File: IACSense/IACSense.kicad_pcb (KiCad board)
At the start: 2 copper layers, 56.6 x 87.4 mm, 75 parts, among them P1 IN, P2 OUT, P3 zcd, P4 event, P5 Prog, P7 I2C, U1 MCP39F521, U2 MCP970x, U3 MCP1754ST-3302E/CB, U4 PIC16F18323_QFN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

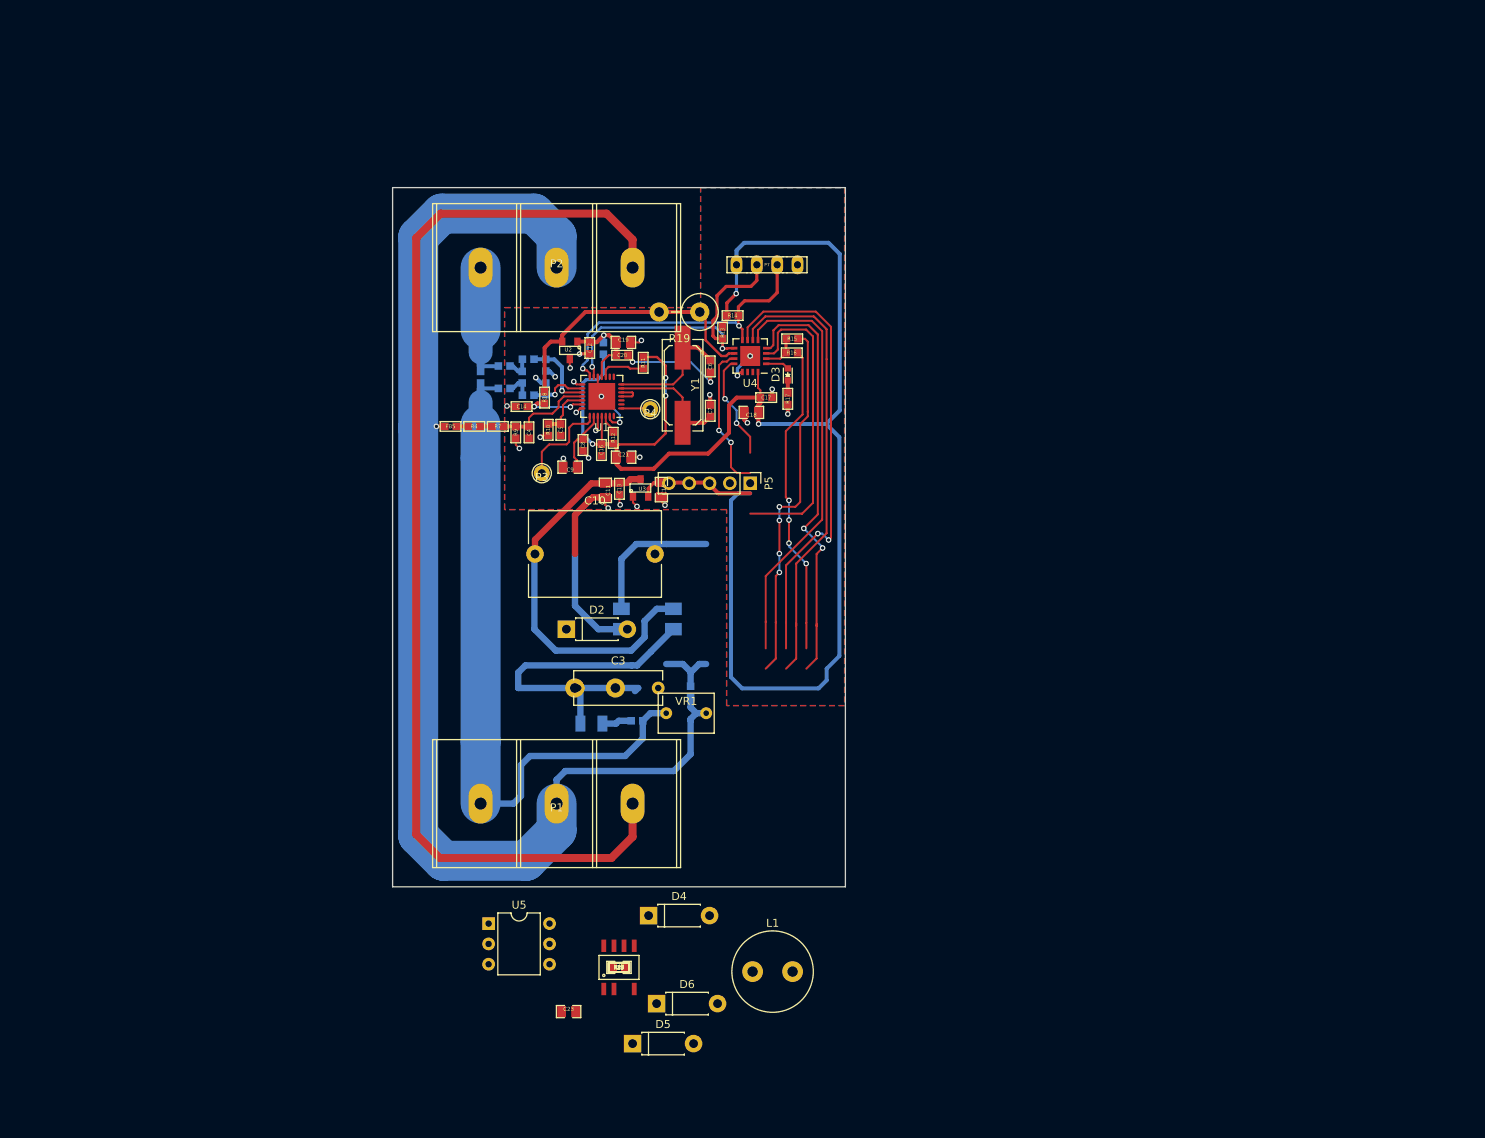
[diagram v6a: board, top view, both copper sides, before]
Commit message: Update IACSense layout
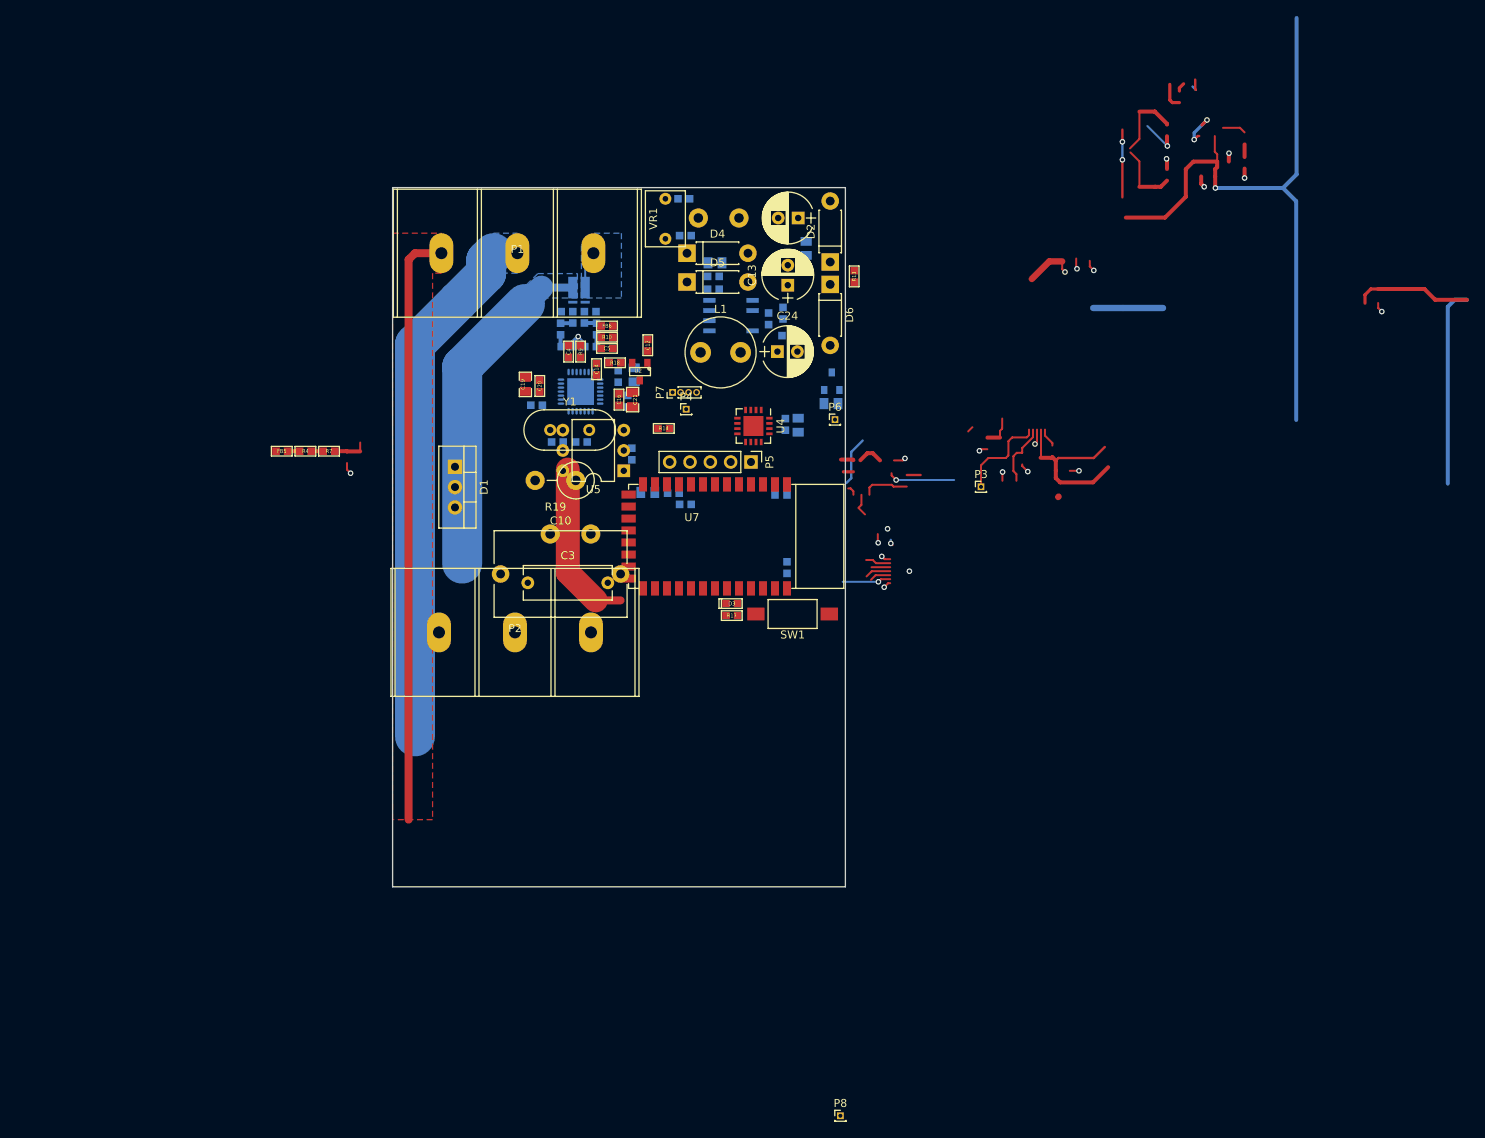
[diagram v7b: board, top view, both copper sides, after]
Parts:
- removed R15: nc, Yame_library:SM0603-MR
- removed R16: 0, Yame_library:SM0603-MR
- added C24: 100u_25V, Capacitors_THT:CP_Radial_D6.3mm_P2.50mm, F.Cu at (228.1, 72.5)
- added C25: C, Yame_library:SM0603-MR, B.Cu at (216.6, 91.6)
- added P6: +3.3v, Pin_Headers:Pin_Header_Straight_1x01_Pitch1.00mm, F.Cu at (235.3, 81.0)
- added P8: Test, Pin_Headers:Pin_Header_Straight_1x01_Pitch1.00mm, F.Cu at (236.0, 168.0)
- added R21: 100, Yame_library:SM0805-MR, B.Cu at (231.7, 59.6)
- added R26: R, Yame_library:SM0603-MR, B.Cu at (229.3, 89.7)
- added R27: R, Yame_library:SM0603-MR, B.Cu at (227.8, 89.7)
- added R28: R, Yame_library:SM0603-MR, B.Cu at (215.1, 90.2)
- added R29: R, Yame_library:SM0603-MR, B.Cu at (229.3, 99.5)
- added SW1: SW_Push, Buttons_Switches_SMD:SW_SPST_FSMSM, F.Cu at (230.0, 105.3)
- added U7: HC-05_Bluetooth_Module, Yame_library:HM-10_BLE, F.Cu at (211.3, 89.1)
- C11: value 1u_400V -> ECA-2GM010; footprint Yame_library:SM0805-MR -> Capacitors_THT:CP_Radial_D6.3mm_P2.50mm
- C13: value 1u_400V -> ECA-2GM010; footprint Yame_library:SM0603-MR -> Capacitors_THT:CP_Radial_D6.3mm_P2.50mm
- C15, C17, C18, C22, C23, C26, C6, C7, C8, C9, R22, R23, R24, R25, U1, U6: moved to B.Cu
- D1: value Q_TRIAC_AAG -> Q_TRIAC; footprint Yame_library:MBxS -> TO_SOT_Packages_THT:TO-220-3_Vertical; moved to F.Cu
- D3: footprint LEDs:LED_0603 -> Yame_library:SM0603-LED-MR
- L1: footprint Inductors_THT:L_Radial_D10.0mm_P5.00mm_Fastron_07M -> Inductors_THT:L_Radial_D8.7mm_P5.00mm_Fastron_07HCP
- P3, P4: footprint Yame_library:Test_Point_T_H -> Pin_Headers:Pin_Header_Straight_1x01_Pitch1.00mm
- P7: footprint Yame_library:HE10_14-4C-2.54-MR -> Pin_Headers:Pin_Header_Straight_1x04_Pitch1.00mm
- R11, R12: value 1k -> 4k7; moved to B.Cu
- R2: footprint Yame_library:SM1206-MR -> FC4L32
- R20: footprint Yame_library:SM0603-MR -> Resistors_THT:R_Axial_DIN0414_L11.9mm_D4.5mm_P5.08mm_Vertical
- U3: value MCP1754ST-3302E/CB -> AP2120N-3.3TRG1; moved to B.Cu
- Y1: footprint Crystals:Q_49U3HMS -> Crystals:Crystal_HC49-4H_Vertical
- moved D5 95.4 mm to (216.8, 63.8)
- moved C23 95.4 mm to (220.3, 61.4), turned to 180 degrees
- moved D6 92.5 mm to (234.7, 64.1), turned to 270 degrees
- moved R22 87.2 mm to (220.1, 63.1), turned to 180 degrees
- moved C22 85.6 mm to (220.1, 64.7), turned to 180 degrees
- moved R24 84.3 mm to (228.8, 67.7), turned to 270 degrees
- moved R23 83.2 mm to (227.0, 68.4), turned to 270 degrees
- moved D4 82.9 mm to (216.8, 60.2)
- moved U6 82.7 mm to (222.3, 68.0), turned to 270 degrees
- moved R25 81.7 mm to (229.4, 70.5)
- moved FB6 80.2 mm to (206.8, 69.3)
- moved L1 77.7 mm to (218.5, 72.6)
- moved P1 69.0 mm to (195.6, 60.2), turned to 180 degrees
- moved VR1 61.9 mm to (214.1, 55.9), turned to 270 degrees
- moved FB1 61.7 mm to (216.4, 53.4), turned to 0 degrees
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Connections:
- C10 pad 1: /Line -> /Line_S
- C11 pad 2: Net-(C11-Pad2) -> GND
- C12 pad 1: /3.3A -> /3.3D
- C13 pad 2: Net-(C11-Pad2) -> GND
- C3 pad 1: /Line -> /Line_S
- D1 pad 1: Net-(D1-Pad1) -> /Line_S
- D1 pad 2: /Line -> /Line_Out
- D4 pad 2: Net-(C11-Pad2) -> GND
- D5 pad 2: Net-(C11-Pad2) -> GND
- FB1 pad 1: /Line -> /Neutral
- FB2 pad 2: /Neutral -> /Line
- FB5 pad 2: /Line -> /Neutral
- P1 pad 1: Net-(P1-Pad1) -> /Line
- P1 pad 2: /Line -> /Neutral
- P2 pad 1: /Neutral -> /Line_Out
- P2 pad 2: Net-(D1-Pad1) -> /Neutral
- P3 pad 1: Net-(P3-Pad1) -> /ZCD
- P4 pad 1: Net-(P4-Pad1) -> /Event
- R11 pad 1: /3.3D -> /3.3A
- R19 pad 1: Net-(D1-Pad1) -> /Line_Out
- R2 pad 1: Net-(P1-Pad1) -> /Line_S
- R25 pad 2: Net-(C11-Pad2) -> GND
- U1 pad 1: Net-(P4-Pad1) -> /Event
- U1 pad 22: Net-(P3-Pad1) -> /ZCD
- U2 pad 1: /3.3A -> /3.3D
- U4 pad 1: Net-(R15-Pad1) -> /Event
- U4 pad 7: Net-(U4-Pad7) -> /ZCD
- VR1 pad 1: /Line -> /Neutral
- VR1 pad 2: /Neutral -> /Line
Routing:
- net (no net): track 0.00 -> 294.3 mm, vias 0 -> 29
- net /3.3D: track 210.3 -> 0.00 mm, vias 5 -> 0
- net /Line: track 209.9 -> 4.72 mm, vias 1 -> 0
- net /Neutral: track 164.4 -> 67.5 mm
- net /Ground: track 12.0 -> 74.4 mm
- net Net-(U4-Pad7): track 58.1 -> 0.00 mm, vias 2 -> 0
- net /Out_SW: track 56.7 -> 0.00 mm
- net /Rx_BL: track 53.7 -> 0.00 mm, vias 2 -> 0
- net /Tx_BL: track 52.8 -> 0.00 mm
- net GND: track 52.7 -> 3.12 mm, vias 26 -> 1
- net Net-(FB3-Pad1): track 48.1 -> 0.00 mm
- net /IRQ: track 45.6 -> 0.00 mm, vias 4 -> 0
- net /Line_S: track 0.00 -> 42.6 mm
- net /SDA: track 39.6 -> 0.00 mm, vias 2 -> 0
- net /CE: track 39.1 -> 0.00 mm, vias 4 -> 0
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- added copper zone on F.Cu, net /Ground
- added copper zone on B.Cu, net /Line
- added copper zone on B.Cu, net /Line_S
- added copper zone on B.Cu, net /Neutral
- removed copper zone on B.Cu, net GND
- removed copper zone on F.Cu, net GND
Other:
- net class AC added: clearance 0.4, trace_width 0.25, via_dia 0.7, via_drill 0.4

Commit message: Update IACSense
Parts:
- removed C10: 100n, Capacitors_THT:C_Rect_L16.5mm_W10.7mm_P15.00mm_MKT
- added R15: R, Yame_library:SM0201-MR, F.Cu at (220.0, 84.0)
- added R16: R, Yame_library:SM0201-MR, F.Cu at (224.7, 78.3)
- C26, R1: moved to F.Cu
- C3: footprint Capacitors_THT:C_Rect_L11.0mm_W4.2mm_P10.00mm_MKT -> Capacitors_THT:C_Rect_L13.0mm_W6.0mm_P10.00mm_FKS3_FKP3_MKS4
- moved P8 87.2 mm to (221.3, 82.1)
- moved P3 35.1 mm to (219.3, 82.0)
- moved R13 29.5 mm to (213.1, 79.3)
- moved C26 23.4 mm to (234.7, 95.2), turned to 90 degrees
- moved R26 23.1 mm to (232.5, 112.6), turned to 0 degrees
- moved R27 21.9 mm to (232.5, 111.1), turned to 0 degrees
- moved U7 21.9 mm to (232.5, 94.6), turned to 270 degrees
- moved U5 17.8 mm to (194.3, 77.3), turned to 270 degrees
- moved R28 16.8 mm to (230.5, 96.8), turned to 270 degrees
- moved SW1 15.2 mm to (214.9, 107.4), turned to 90 degrees
- moved R29 14.6 mm to (221.6, 111.9)
- moved C25 13.0 mm to (228.2, 97.5), turned to 180 degrees
- moved D3 8.88 mm to (215.0, 99.1), turned to 0 degrees
- moved R17 8.88 mm to (215.0, 100.6), turned to 180 degrees
- moved R19 8.21 mm to (194.7, 89.0), turned to 270 degrees
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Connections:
- U4 pad 10: /SCL -> Net-(R15-Pad1)
- U4 pad 2: /SDA -> Net-(R16-Pad1)
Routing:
- net (no net): track 294.3 -> 1.51 mm, vias 29 -> 1
- net GND: track 3.12 -> 33.9 mm, vias 1 -> 2
- net /Ground: track 74.4 -> 46.4 mm
- net Net-(C22-Pad2): track 0.00 -> 26.8 mm
- net Net-(R8-Pad1): track 20.9 -> 0.00 mm
- net Net-(C23-Pad1): track 0.00 -> 20.3 mm
- net Net-(C13-Pad1): track 0.00 -> 17.9 mm, vias 0 -> 1
- net /+5V: track 0.00 -> 15.5 mm
- net Net-(D2-Pad2): track 0.00 -> 14.1 mm
- net /ZCD: track 12.0 -> 0.00 mm
- net /Line: track 4.72 -> 16.4 mm
- net /Neutral: track 67.5 -> 76.3 mm
- net Net-(C11-Pad1): track 0.00 -> 8.43 mm
- net Net-(C22-Pad1): track 0.00 -> 7.36 mm
- net Net-(C5-Pad1): track 0.00 -> 5.90 mm, vias 0 -> 1
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- removed copper zone on F.Cu, net /Ground
- removed copper zone on B.Cu, net /Neutral
